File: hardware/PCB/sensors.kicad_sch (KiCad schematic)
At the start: 25 parts, among them IC1 IIS2MDCTR, IC2 BNO085, J1 GPS, U11 INA219BxDCN, U5 LSM6DSOXTR, U6 INA219BxDCN, Y1 Crystal

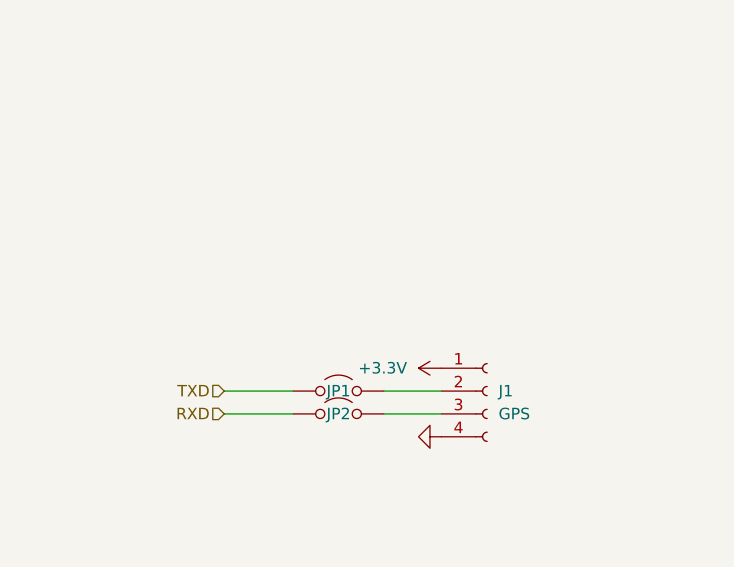
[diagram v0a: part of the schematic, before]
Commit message: Added connection for external IMU to PCB
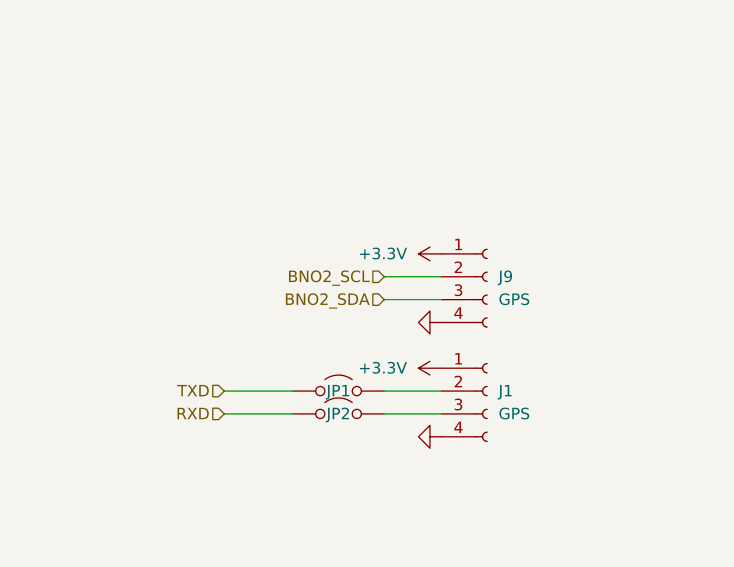
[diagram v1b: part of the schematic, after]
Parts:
- added J9: GPS, Connector_PinSocket_2.54mm:PinSocket_1x04_P2.54mm_Vertical, symbol Connector:Conn_01x04_Socket
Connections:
- net +3.3V: now also J9.1 (Pin_1)
- net GND: now also J9.4 (Pin_4)
- new net BNO2_SCL: J9.2 (Pin_2)
- new net BNO2_SDA: J9.3 (Pin_3)
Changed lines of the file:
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@@
 	(wire
 		(pts
+			(xy 224.79 123.19) (xy 231.14 123.19)
+		)
+		(stroke
+			(width 0)
+			(type default)
+		)
+	)
+	(wire
+		(pts
 			(xy 135.89 176.53) (xy 135.89 177.8)
 		)
@@
 	(wire
 		(pts
+			(xy 224.79 125.73) (xy 231.14 125.73)
+		)
+		(stroke
+			(width 0)
+			(type default)
+		)
+	)
+	(wire
+		(pts
 			(xy 44.45 58.42) (xy 52.07 58.42)
 		)
@@
 		)
 	)
+	(hierarchical_label "BNO2_SCL"
+		(shape input)
+		(at 224.79 123.19 180)
+		(effects
+			(font
+				(size 1.27 1.27)
+			)
+			(justify right)
+		)
+	)
 	(hierarchical_label "RXD"
 		(shape input)
@@
 		)
 	)
+	(hierarchical_label "BNO2_SDA"
+		(shape input)
+		(at 224.79 125.73 180)
+		(effects
+			(font
+				(size 1.27 1.27)
+			)
+			(justify right)
+		)
+	)
 	(symbol
 		(lib_id "power:GND")
@@
 	)
 	(symbol
+		(lib_id "power:GND")
+		(at 231.14 128.27 270)
+		(unit 1)
+		(exclude_from_sim no)
+		(in_bom yes)
+		(on_board yes)
+		(dnp no)
+		(fields_autoplaced yes)
+		(property "Reference" "#PWR079"
+			(at 224.79 128.27 0)
+			(effects
+				(font
+					(size 1.27 1.27)
+				)
+				(hide yes)
+			)
+		)
+		(property "Value" "GND"
+			(at 227.33 128.2699 90)
+			(effects
+				(font
+					(size 1.27 1.27)
+				)
+				(justify right)
+				(hide yes)
+			)
+		)
+		(property "Footprint" ""
+			(at 231.14 128.27 0)
+			(effects
+				(font
+					(size 1.27 1.27)
+				)
+				(hide yes)
+			)
+		)
+		(property "Datasheet" ""
+			(at 231.14 128.27 0)
+			(effects
+				(font
+					(size 1.27 1.27)
+				)
+				(hide yes)
+			)
+		)
+		(property "Description" "Power symbol creates a global label with name \"GND\" , ground"
+			(at 231.14 128.27 0)
+			(effects
+				(font
+					(size 1.27 1.27)
+				)
+				(hide yes)
+			)
+		)
+		(pin "1"
+		)
+		(instances
+			(project "Startracker"
+				(path "/45ea479c-a8ef-4c14-88b0-391ede4fd156/e8f32813-0603-4e85-9176-ac6a48f0a36f"
+					(reference "#PWR079")
+					(unit 1)
+				)
+			)
+		)
+	)
+	(symbol
 		(lib_id "power:+3.3V")
 		(at 118.11 154.94 0)
@@
 	)
 	(symbol
+		(lib_id "Connector:Conn_01x04_Socket")
+		(at 236.22 123.19 0)
+		(unit 1)
+		(exclude_from_sim no)
+		(in_bom yes)
+		(on_board yes)
+		(dnp no)
+		(fields_autoplaced yes)
+		(property "Reference" "J9"
+			(at 237.49 123.1899 0)
+			(effects
+				(font
+					(size 1.27 1.27)
+				)
+				(justify left)
+			)
+		)
+		(property "Value" "GPS"
+			(at 237.49 125.7299 0)
+			(effects
+				(font
+					(size 1.27 1.27)
+				)
+				(justify left)
+			)
+		)
+		(property "Footprint" "Connector_PinSocket_2.54mm:PinSocket_1x04_P2.54mm_Vertical"
+			(at 236.22 123.19 0)
+			(effects
+				(font
+					(size 1.27 1.27)
+				)
+				(hide yes)
+			)
+		)
+		(property "Datasheet" "~"
+			(at 236.22 123.19 0)
+			(effects
+				(font
+					(size 1.27 1.27)
+				)
+				(hide yes)
+			)
+		)
+		(property "Description" "Generic connector, single row, 01x04, script generated"
+			(at 236.22 123.19 0)
+			(effects
+				(font
+					(size 1.27 1.27)
+				)
+				(hide yes)
+			)
+		)
+		(pin "4"
+		)
+		(pin "3"
+		)
+		(pin "2"
+		)
+		(pin "1"
+		)
+		(instances
+			(project "Startracker"
+				(path "/45ea479c-a8ef-4c14-88b0-391ede4fd156/e8f32813-0603-4e85-9176-ac6a48f0a36f"
+					(reference "J9")
+					(unit 1)
+				)
+			)
+		)
+	)
+	(symbol
 		(lib_id "Device:C_Small")
 		(at 116.84 74.93 180)
@@
 					(unit 1)
 				)
+			)
+		)
+	)
+	(symbol
+		(lib_id "power:+3.3V")
+		(at 231.14 120.65 90)
+		(unit 1)
+		(exclude_from_sim no)
+		(in_bom yes)
+		(on_board yes)
+		(dnp no)
+		(fields_autoplaced yes)
+		(property "Reference" "#PWR025"
+			(at 234.95 120.65 0)
+			(effects
+				(font
+					(size 1.27 1.27)
+				)
+				(hide yes)
+			)
+		)
+		(property "Value" "+3.3V"
+			(at 227.33 120.6499 90)
+			(effects
+				(font
+					(size 1.27 1.27)
+				)
+				(justify left)
+			)
+		)
+		(property "Footprint" ""
+			(at 231.14 120.65 0)
+			(effects
+				(font
+					(size 1.27 1.27)
+				)
+				(hide yes)
+			)
+		)
+		(property "Datasheet" ""
+			(at 231.14 120.65 0)
+			(effects
+				(font
+					(size 1.27 1.27)
+				)
+				(hide yes)
+			)
+		)
+		(property "Description" "Power symbol creates a global label with name \"+3.3V\""
+			(at 231.14 120.65 0)
+			(effects
+				(font
+					(size 1.27 1.27)
+				)
+				(hide yes)
+			)
+		)
+		(pin "1"
+		)
+		(instances
+			(project "Startracker"
+				(path "/45ea479c-a8ef-4c14-88b0-391ede4fd156/e8f32813-0603-4e85-9176-ac6a48f0a36f"
+					(reference "#PWR025")
+					(unit 1)
+				)

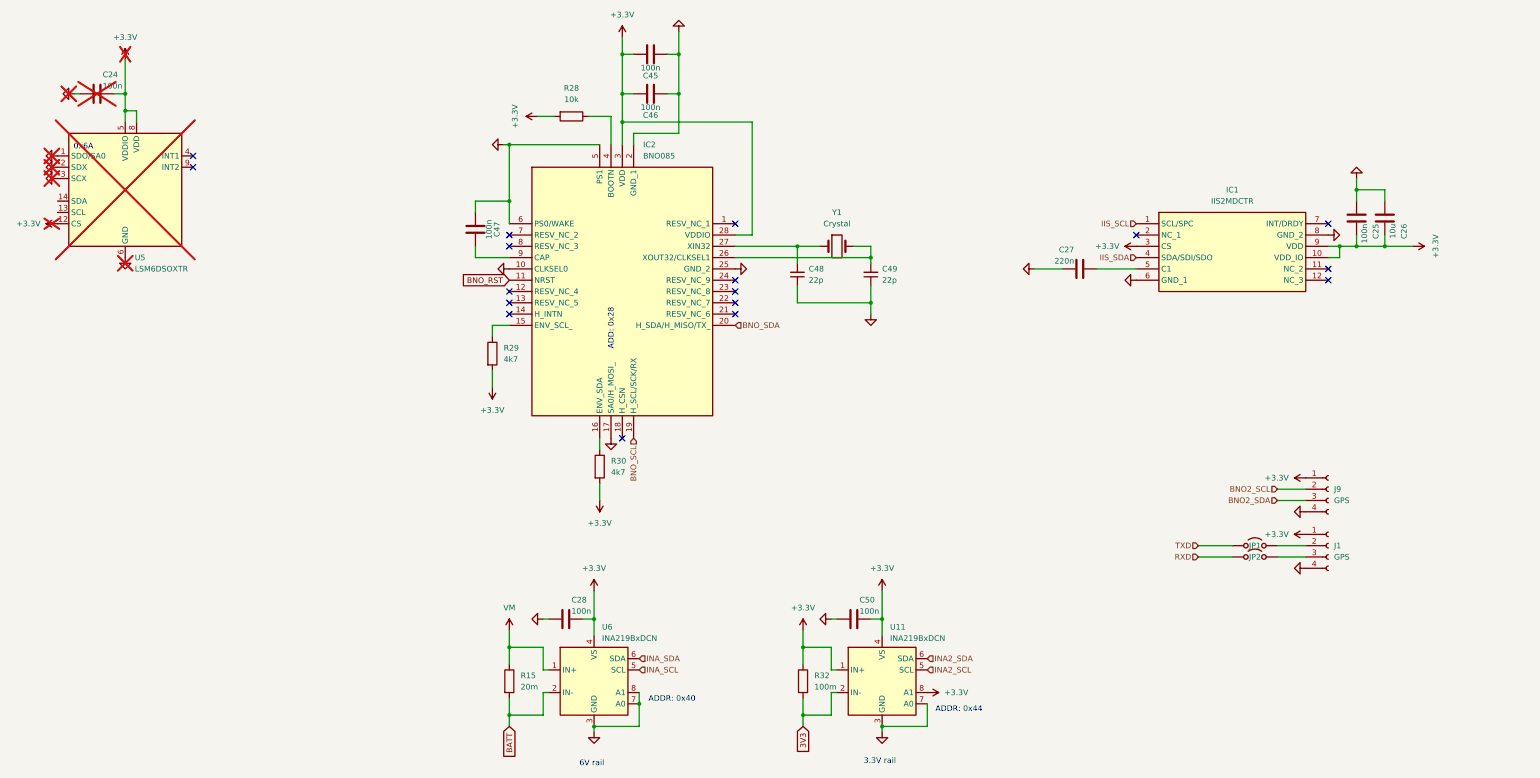
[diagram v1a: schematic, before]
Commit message: Finished schematic for LoRa, added BME280
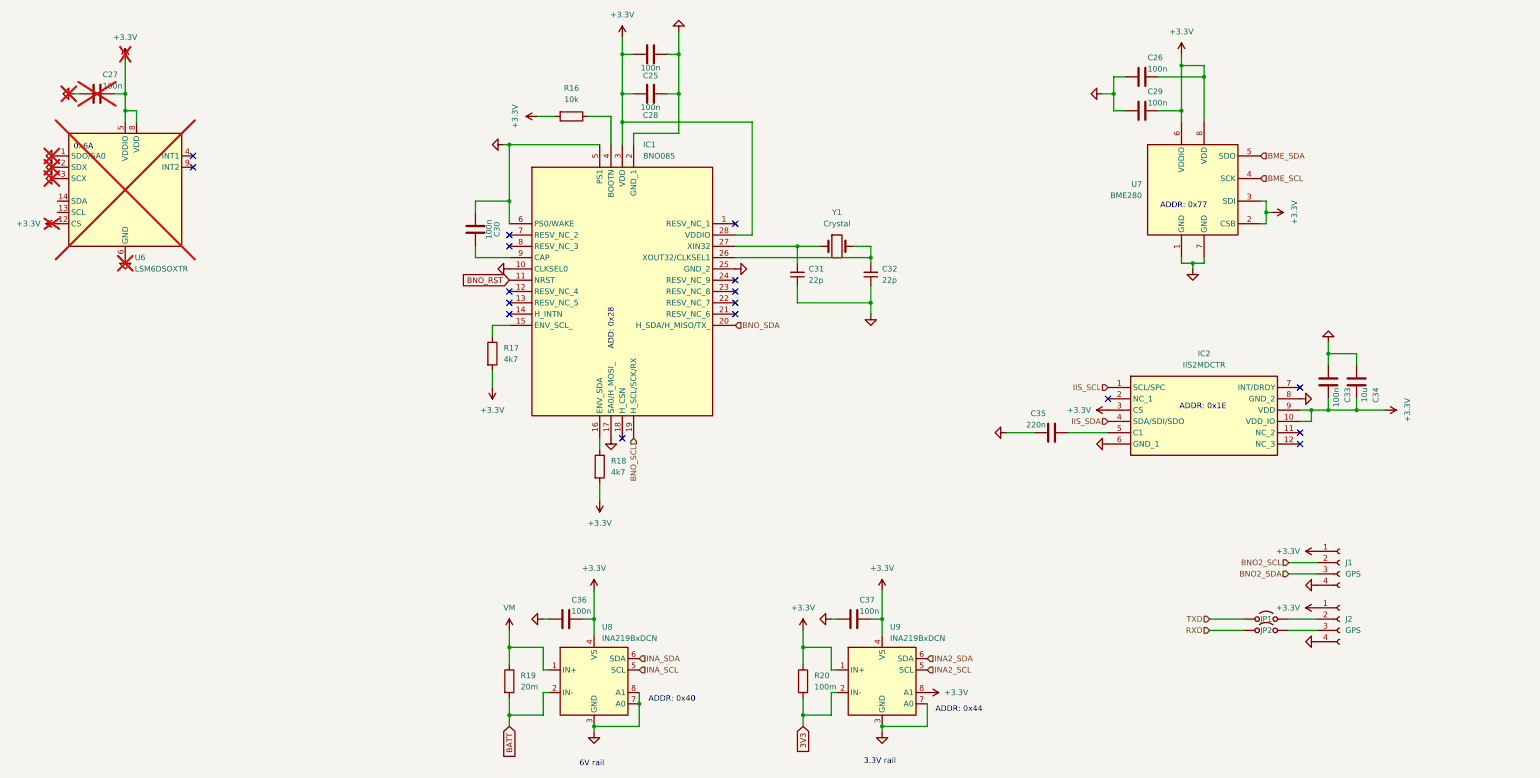
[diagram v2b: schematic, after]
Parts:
- added C26, C29: 100n, Capacitor_SMD:C_1206_3216Metric_Pad1.33x1.80mm_HandSolder, symbol Device:C
- added U7: BME280, Package_LGA:Bosch_LGA-8_2.5x2.5mm_P0.65mm_ClockwisePinNumbering, symbol Sensor:BME280
- renumbered C45 to C25, C24 to C27, C46 to C28, C47 to C30, C48 to C31, C49 to C32, C25 to C33, C26 to C34, C27 to C35, C28 to C36, C50 to C37, IC2 to IC1, IC1 to IC2, J9 to J1, J1 to J2, R28 to R16, R29 to R17, R30 to R18, R15 to R19, R32 to R20, U5 to U6, U6 to U8, U11 to U9
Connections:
- net +3.3V: now also C26.2, C29.2, U7.2 (CSB), U7.3 (SDI), U7.6 (VDDIO), U7.8 (VDD)
- net GND_1: now also C26.1, C29.1, U7.1 (GND), U7.7 (GND)
- new net BME_SCL: U7.4 (SCK)
- new net BME_SDA: U7.5 (SDO)
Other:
- note added: "ADDR: 0x1E"
- note added: "ADDR: 0x77"
- moved on the sheet: C33, C34, C35, IC2, J1, J2, JP1, JP2

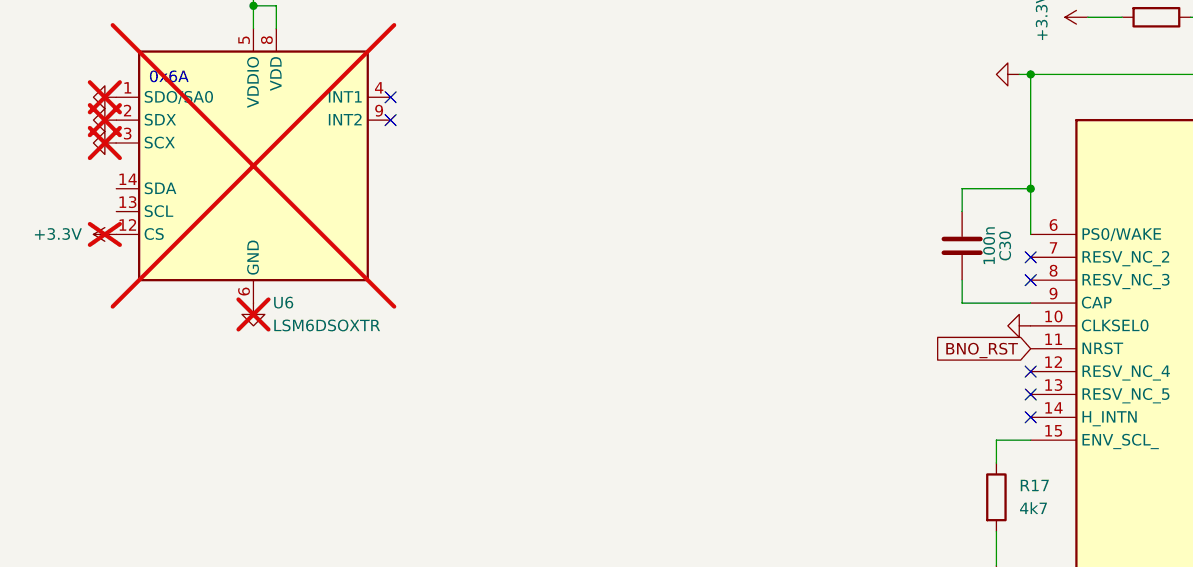
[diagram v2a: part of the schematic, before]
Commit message: Rerouted changes on the PCB layout, Routed LoRa
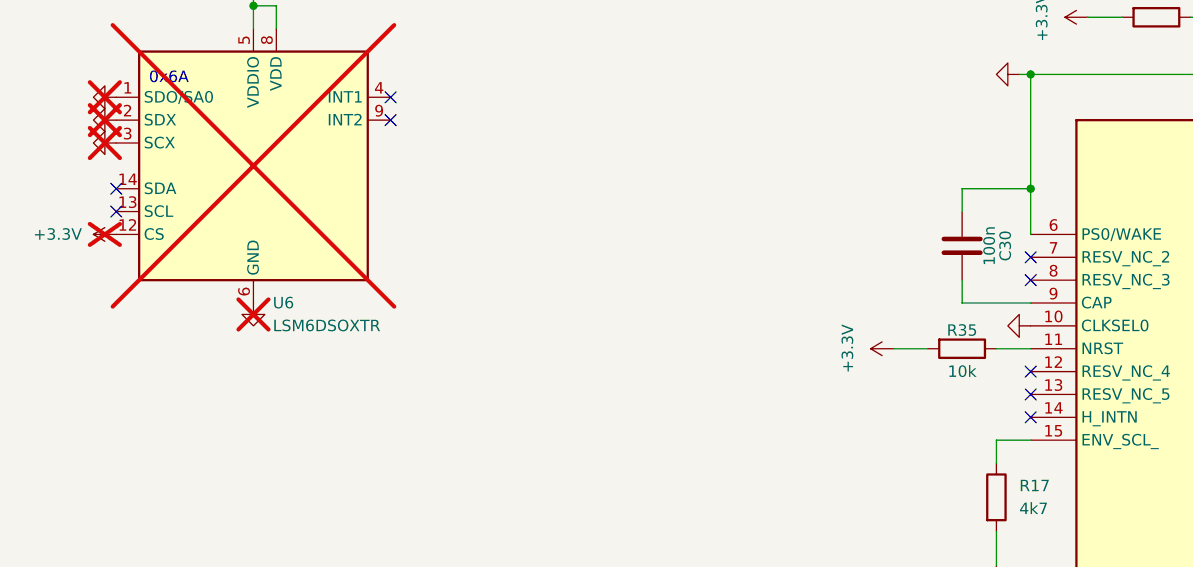
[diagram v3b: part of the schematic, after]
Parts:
- added R35: 10k, Capacitor_SMD:C_1206_3216Metric_Pad1.33x1.80mm_HandSolder, symbol Device:R
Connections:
- net +3.3V: now also R35.2
- net BNO_RST: no longer names the net of IC1.11 (NRST)
- net BNO_RST: now also R35.1
- no-connect marks 17 -> 19
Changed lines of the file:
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@@
 	)
 	(no_connect
+		(at -49.53 60.96)
+	)
+	(no_connect
 		(at 52.07 83.82)
 	)
@@
 	)
 	(no_connect
+		(at -49.53 58.42)
+	)
+	(no_connect
 		(at 229.87 110.49)
 	)
@@
 	(wire
 		(pts
+			(xy 36.83 76.2) (xy 40.64 76.2)
+		)
+		(stroke
+			(width 0)
+			(type default)
+		)
+	)
+	(wire
+		(pts
 			(xy 90.17 25.4) (xy 87.63 25.4)
 		)
@@
 	(wire
 		(pts
+			(xy 48.26 76.2) (xy 52.07 76.2)
+		)
+		(stroke
+			(width 0)
+			(type default)
+		)
+	)
+	(wire
+		(pts
 			(xy 242.57 92.71) (xy 236.22 92.71)
 		)
@@
 		)
 	)
-	(global_label "BNO_RST"
-		(shape input)
-		(at 52.07 76.2 180)
-		(fields_autoplaced yes)
-		(effects
-			(font
-				(size 1.27 1.27)
-			)
-			(justify right)
-		)
-		(property "Intersheetrefs" "${INTERSHEET_REFS}"
-			(at 40.7391 76.2 0)
-			(effects
-				(font
-					(size 1.27 1.27)
-				)
-				(justify right)
-				(hide yes)
-			)
-		)
-	)
 	(global_label "BATT"
 		(shape input)
@@
 	)
 	(symbol
+		(lib_id "Device:R")
+		(at 44.45 76.2 270)
+		(unit 1)
+		(exclude_from_sim no)
+		(in_bom yes)
+		(on_board yes)
+		(dnp no)
+		(property "Reference" "R35"
+			(at 44.45 74.168 90)
+			(effects
+				(font
+					(size 1.27 1.27)
+				)
+			)
+		)
+		(property "Value" "10k"
+			(at 44.45 78.74 90)
+			(effects
+				(font
+					(size 1.27 1.27)
+				)
+			)
+		)
+		(property "Footprint" "Capacitor_SMD:C_1206_3216Metric_Pad1.33x1.80mm_HandSolder"
+			(at 44.45 74.422 90)
+			(effects
+				(font
+					(size 1.27 1.27)
+				)
+				(hide yes)
+			)
+		)
+		(property "Datasheet" "~"
+			(at 44.45 76.2 0)
+			(effects
+				(font
+					(size 1.27 1.27)
+				)
+				(hide yes)
+			)
+		)
+		(property "Description" "Resistor"
+			(at 44.45 76.2 0)
+			(effects
+				(font
+					(size 1.27 1.27)
+				)
+				(hide yes)
+			)
+		)
+		(property "Sim.Device" ""
+			(at 44.45 76.2 0)
+			(effects
+				(font
+					(size 1.27 1.27)
+				)
+				(hide yes)
+			)
+		)
+		(property "TAPE_REEL" ""
+			(at 44.45 76.2 0)
+			(effects
+				(font
+					(size 1.27 1.27)
+				)
+				(hide yes)
+			)
+		)
+		(property "VOLUME" ""
+			(at 44.45 76.2 0)
+			(effects
+				(font
+					(size 1.27 1.27)
+				)
+				(hide yes)
+			)
+		)
+		(pin "2"
+		)
+		(pin "1"
+		)
+		(instances
+			(project "Startracker"
+				(path "/45ea479c-a8ef-4c14-88b0-391ede4fd156/e8f32813-0603-4e85-9176-ac6a48f0a36f"
+					(reference "R35")
+					(unit 1)
+				)
+			)
+		)
+	)
+	(symbol
 		(lib_id "power:+3.3V")
 		(at 223.52 60.96 270)
@@
 					(unit 1)
 				)
+			)
+		)
+	)
+	(symbol
+		(lib_id "power:+3.3V")
+		(at 36.83 76.2 90)
+		(unit 1)
+		(exclude_from_sim no)
+		(in_bom yes)
+		(on_board yes)
+		(dnp no)
+		(fields_autoplaced yes)
+		(property "Reference" "#PWR0120"
+			(at 40.64 76.2 0)
+			(effects
+				(font
+					(size 1.27 1.27)
+				)
+				(hide yes)
+			)
+		)
+		(property "Value" "+3.3V"
+			(at 31.75 76.2 0)
+			(effects
+				(font
+					(size 1.27 1.27)
+				)
+			)
+		)
+		(property "Footprint" ""
+			(at 36.83 76.2 0)
+			(effects
+				(font
+					(size 1.27 1.27)
+				)
+				(hide yes)
+			)
+		)
+		(property "Datasheet" ""
+			(at 36.83 76.2 0)
+			(effects
+				(font
+					(size 1.27 1.27)
+				)
+				(hide yes)
+			)
+		)
+		(property "Description" "Power symbol creates a global label with name \"+3.3V\""
+			(at 36.83 76.2 0)
+			(effects
+				(font
+					(size 1.27 1.27)
+				)
+				(hide yes)
+			)
+		)
+		(pin "1"
+		)
+		(instances
+			(project "Startracker"
+				(path "/45ea479c-a8ef-4c14-88b0-391ede4fd156/e8f32813-0603-4e85-9176-ac6a48f0a36f"
+					(reference "#PWR0120")
+					(unit 1)
+				)

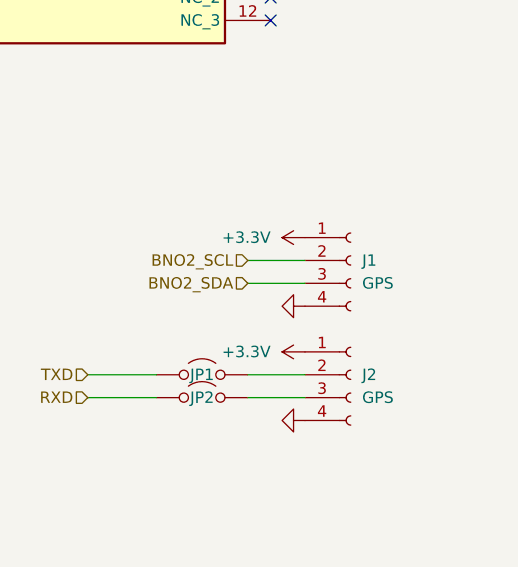
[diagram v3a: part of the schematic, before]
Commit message: Completed placement of components on PCB
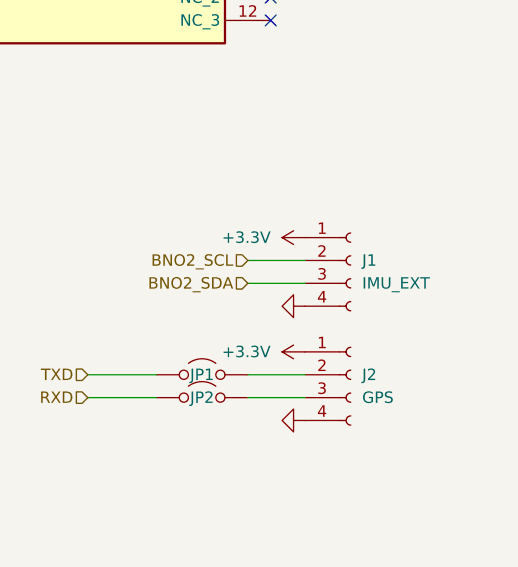
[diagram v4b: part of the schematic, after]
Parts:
- J1: value GPS -> IMU_EXT
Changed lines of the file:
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@@
 			)
 		)
-		(property "Value" "GPS"
+		(property "Value" "IMU_EXT"
 			(at 240.03 142.2399 0)
 			(effects

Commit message: Finished routing and layout of PCB
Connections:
- net GND: now also C26.1, C29.1, C33.1, C34.1, C35.2, C36.1, C37.1, IC2.6 (GND_1), IC2.8 (GND_2), U7.1 (GND), U7.7 (GND), U8.3 (GND), U8.7 (A0), U8.8 (A1), U9.3 (GND), U9.7 (A0)
- net GND_1: no longer C26.1, C29.1, C33.1, C34.1, C35.2, C36.1, C37.1, IC2.6 (GND_1), IC2.8 (GND_2), U7.1 (GND), U7.7 (GND), U8.3 (GND), U8.7 (A0), U8.8 (A1), U9.3 (GND), U9.7 (A0)
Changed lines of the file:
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@@
 			)
 		)
-		(property "Value" "GND_1"
+		(property "Value" "GND"
 			(at 180.34 34.29 0)
 			(effects
@@
 			)
 		)
-		(property "Value" "GND_1"
+		(property "Value" "GND"
 			(at 234.95 102.87 0)
 			(effects
@@
 			)
 		)
-		(property "Value" "GND_1"
+		(property "Value" "GND"
 			(at 119.38 152.4 0)
 			(effects
@@
 			)
 		)
-		(property "Value" "GND_1"
+		(property "Value" "GND"
 			(at 236.22 85.09 0)
 			(effects
@@
 			)
 		)
-		(property "Value" "GND_1"
+		(property "Value" "GND"
 			(at 205.74 78.74 0)
 			(effects
@@
 			)
 		)
-		(property "Value" "GND_1"
+		(property "Value" "GND"
 			(at 71.12 182.88 0)
 			(effects
@@
 			)
 		)
-		(property "Value" "GND_1"
+		(property "Value" "GND"
 			(at 158.75 110.49 0)
 			(effects
@@
 			)
 		)
-		(property "Value" "GND_1"
+		(property "Value" "GND"
 			(at 54.61 152.4 0)
 			(effects
@@
 			)
 		)
-		(property "Value" "GND_1"
+		(property "Value" "GND"
 			(at 135.89 182.88 0)
 			(effects
@@
 			)
 		)
-		(property "Value" "GND_1"
+		(property "Value" "GND"
 			(at 181.61 113.03 0)
 			(effects
